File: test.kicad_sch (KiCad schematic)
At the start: 31 parts, among them IC3 USBLC6-2SC6, IC4 ESP32-S3-WROOM-1-N16, J1 UART0, SW1 Reset, SW2 Boot, U3 USB-TYPE-C-018, U7 ADC08351CILQX{slash}NOPB, U8 ADC08351CILQX{slash}NOPB

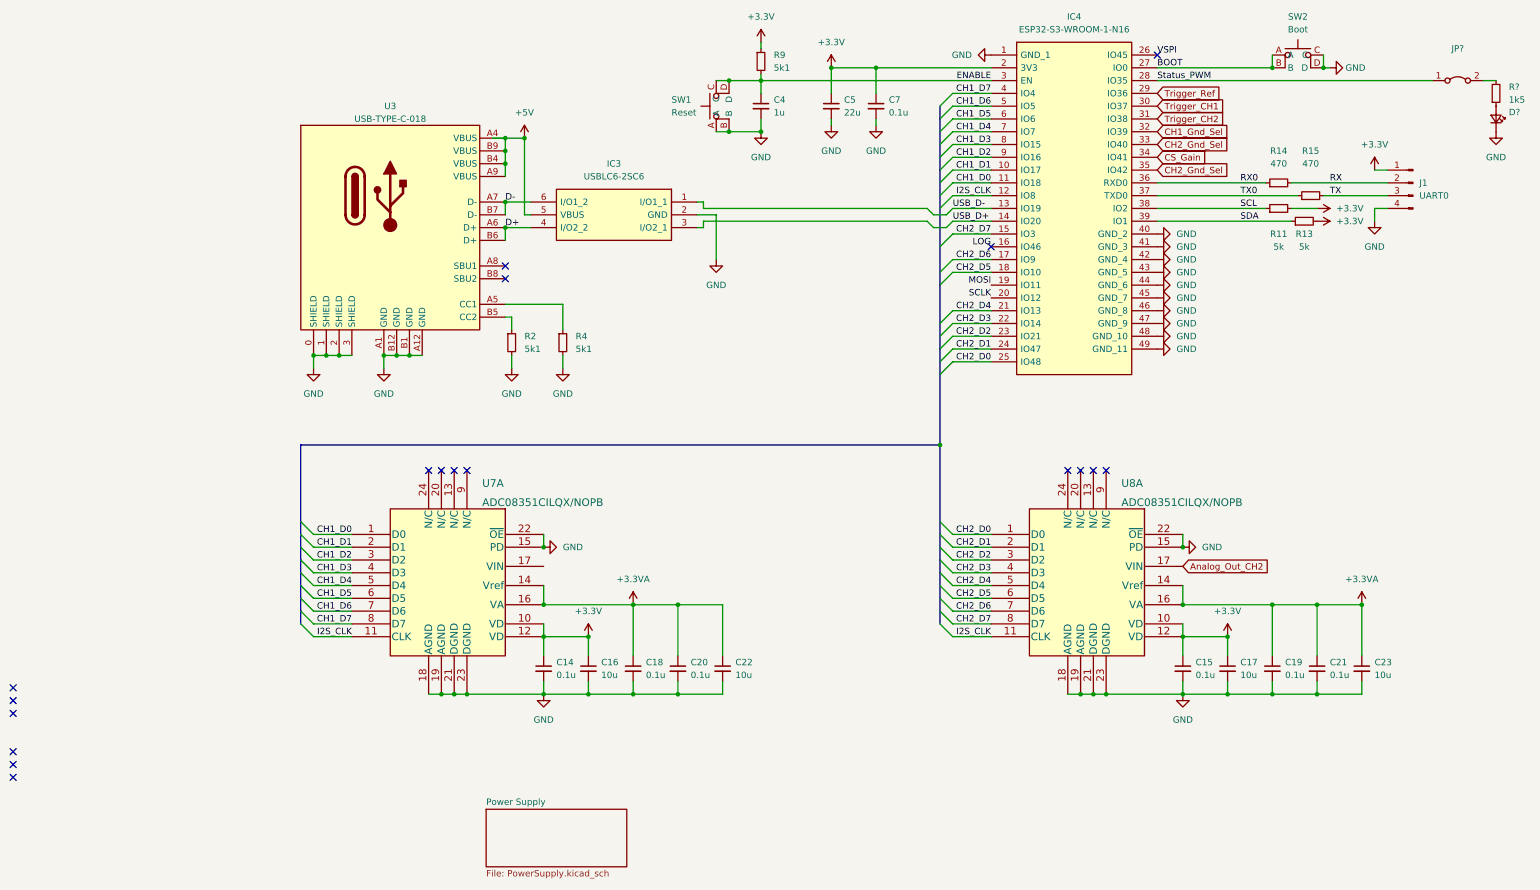
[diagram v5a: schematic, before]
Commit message: resolve DRC on schematic
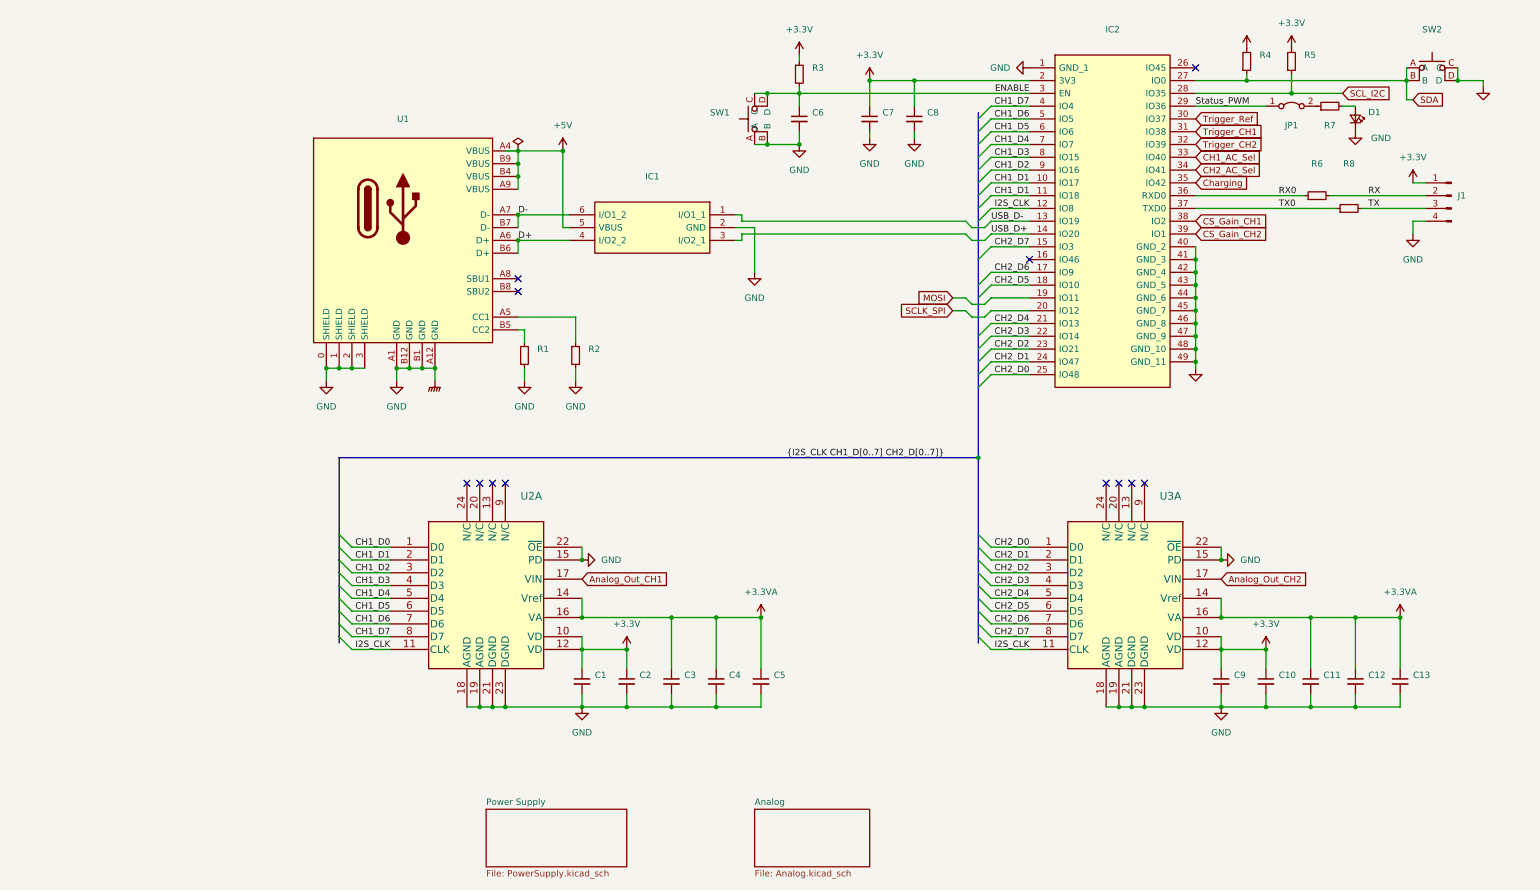
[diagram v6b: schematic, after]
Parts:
- removed R11, R13: 5k, Resistor_SMD:R_0805_2012Metric_Pad1.20x1.40mm_HandSolder, symbol Device:R_Small
- removed R?: 1k5, Resistor_SMD:R_0805_2012Metric_Pad1.20x1.40mm_HandSolder, symbol Device:R_Small
- added R4, R5, R7: (no value), symbol Device:R_Small
- C1: renamed from C14; value 0.1u -> (none); footprint Capacitor_SMD:C_0805_2012Metric_Pad1.18x1.45mm_HandSolder -> (none)
- C10: renamed from C17; value 10u -> (none); footprint Capacitor_SMD:C_0805_2012Metric_Pad1.18x1.45mm_HandSolder -> (none)
- C11: renamed from C19; value 0.1u -> (none); footprint Capacitor_SMD:C_0805_2012Metric_Pad1.18x1.45mm_HandSolder -> (none)
- C12: renamed from C21; value 0.1u -> (none); footprint Capacitor_SMD:C_0805_2012Metric_Pad1.18x1.45mm_HandSolder -> (none)
- C13: renamed from C23; value 10u -> (none); footprint Capacitor_SMD:C_0805_2012Metric_Pad1.18x1.45mm_HandSolder -> (none)
- C2: renamed from C16; value 10u -> (none); footprint Capacitor_SMD:C_0805_2012Metric_Pad1.18x1.45mm_HandSolder -> (none)
- C3: renamed from C18; value 0.1u -> (none); footprint Capacitor_SMD:C_0805_2012Metric_Pad1.18x1.45mm_HandSolder -> (none)
- C4: renamed from C20; value 0.1u -> (none); footprint Capacitor_SMD:C_0805_2012Metric_Pad1.18x1.45mm_HandSolder -> (none)
- C5: renamed from C22; value 10u -> (none); footprint Capacitor_SMD:C_0805_2012Metric_Pad1.18x1.45mm_HandSolder -> (none)
- C6: renamed from C4; value 1u -> (none); footprint Capacitor_SMD:C_0805_2012Metric_Pad1.18x1.45mm_HandSolder -> (none)
- C7: renamed from C5; value 22u -> (none); footprint Capacitor_SMD:C_0805_2012Metric_Pad1.18x1.45mm_HandSolder -> (none)
- C8: renamed from C7; value 0.1u -> (none); footprint Capacitor_SMD:C_0805_2012Metric_Pad1.18x1.45mm_HandSolder -> (none)
- C9: renamed from C15; value 0.1u -> (none); footprint Capacitor_SMD:C_0805_2012Metric_Pad1.18x1.45mm_HandSolder -> (none)
- D1: renamed from D?; footprint LED_SMD:LED_0805_2012Metric_Pad1.15x1.40mm_HandSolder -> (none)
- IC1: renamed from IC3; value USBLC6-2SC6 -> (none); footprint project_library:USBLC6-2SC6 -> (none)
- IC2: renamed from IC4; value ESP32-S3-WROOM-1-N16 -> (none); footprint project_library:ESP32-S3-WROOM-1 -> (none)
- J1: value UART0 -> (none); footprint Connector_PinHeader_2.54mm:PinHeader_1x04_P2.54mm_Vertical -> (none)
- R1: renamed from R2; value 5k1 -> (none); footprint Resistor_SMD:R_0805_2012Metric_Pad1.20x1.40mm_HandSolder -> (none)
- R2: renamed from R4; value 5k1 -> (none); footprint Resistor_SMD:R_0805_2012Metric_Pad1.20x1.40mm_HandSolder -> (none)
- R3: renamed from R9; value 5k1 -> (none); footprint Resistor_SMD:R_0805_2012Metric_Pad1.20x1.40mm_HandSolder -> (none)
- R6: renamed from R14; value 470 -> (none); footprint Resistor_SMD:R_0805_2012Metric_Pad1.20x1.40mm_HandSolder -> (none)
- R8: renamed from R15; value 470 -> (none); footprint Resistor_SMD:R_0805_2012Metric_Pad1.20x1.40mm_HandSolder -> (none)
- SW1: value Reset -> (none); footprint project_library:SW_TS-1187A-B-A-B -> (none)
- SW2: value Boot -> (none); footprint project_library:SW_TS-1187A-B-A-B -> (none)
- U1: renamed from U3; value USB-TYPE-C-018 -> (none); footprint footprint:USB-C_SMD-TYPE-C-31-M-12 -> (none)
- U2: renamed from U7; value ADC08351CILQX/NOPB -> (none); footprint project_library:ADC08351CILQX -> (none)
- U3: renamed from U8; value ADC08351CILQX/NOPB -> (none); footprint project_library:ADC08351CILQX -> (none)
- gave numbers to parts that had none: 1
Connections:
- net BOOT is gone; now on net SDA: IC2.27 (IO0), SW2.A, SW2.B
- net CH1_Gnd_Sel is gone; now on net Trigger_CH2: IC2.32 (IO39)
- net +3V3: now also R4.2, R5.2
- net CH1_D0: no longer IC2.11 (IO18)
- net CH1_D1: now also IC2.11 (IO18)
- net SDA: now also R4.1; no longer IC2.39 (IO1)
- net Status_PWM: now also IC2.29 (IO36); no longer IC2.28 (IO35)
- net Trigger_CH1: now also IC2.31 (IO38); no longer IC2.30 (IO37)
- net Trigger_CH2: no longer IC2.31 (IO38)
- net Trigger_Ref: now also IC2.30 (IO37); no longer IC2.29 (IO36)
- net at JP1.2 (B): now also R7.1
- net at D1.2 (A): now also R7.2
- net Analog_Out_CH1: now reaches U2.17 (VIN)
- net CH2_Gnd_Sel renamed CH1_AC_Sel
- net CH1_AC_Sel: no longer IC2.35 (IO42)
- net CS_Gain renamed CH2_AC_Sel
- net LOG: no longer names the net of IC2.16 (IO46)
- net SCL renamed CS_Gain_CH1
- net SCLK renamed SCLK_SPI
- net VSPI: no longer names the net of IC2.26 (IO45)
- new net CS_Gain_CH2: IC2.39 (IO1)
- new net Charging: IC2.35 (IO42)
- new net SCL_I2C: IC2.28 (IO35), R5.1
- no-connect marks 18 -> 12
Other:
- added sheet Analog (Analog.kicad_sch)
- moved on the sheet: C1, C10, C11, C12, C13, C2, C3, C4, C5, C6, C7, C8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
